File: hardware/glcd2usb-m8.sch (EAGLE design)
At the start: 19 parts, among them IC1 MEGA8-P, Q1 12MHz, T1 BC547

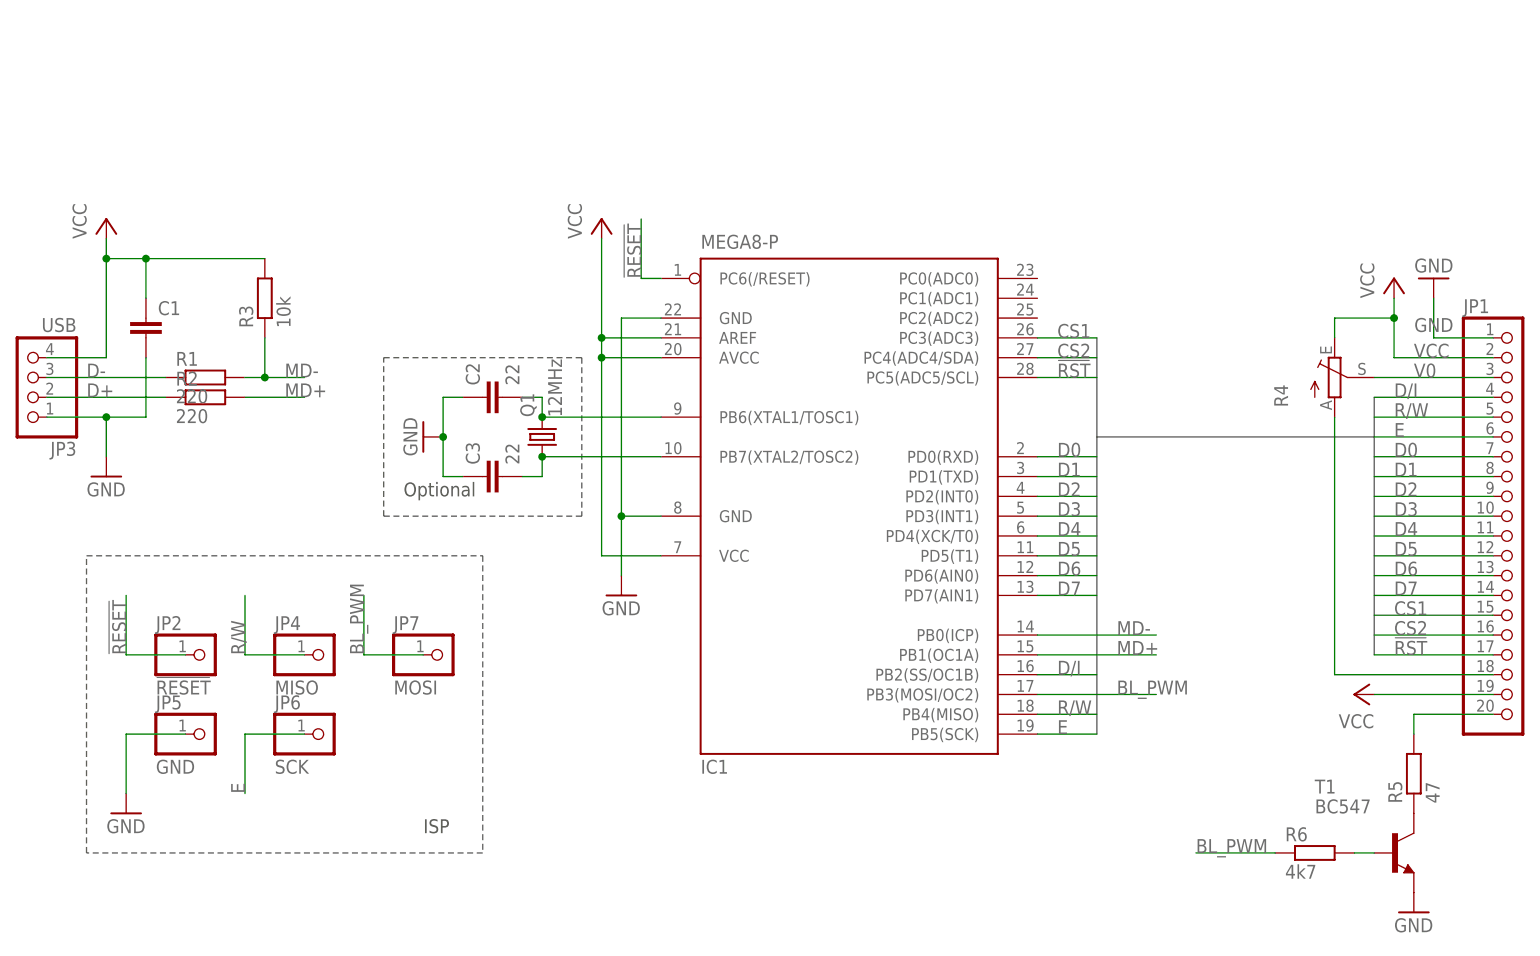
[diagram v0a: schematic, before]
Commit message: use PortC for contntrol (glcd lib limitations)
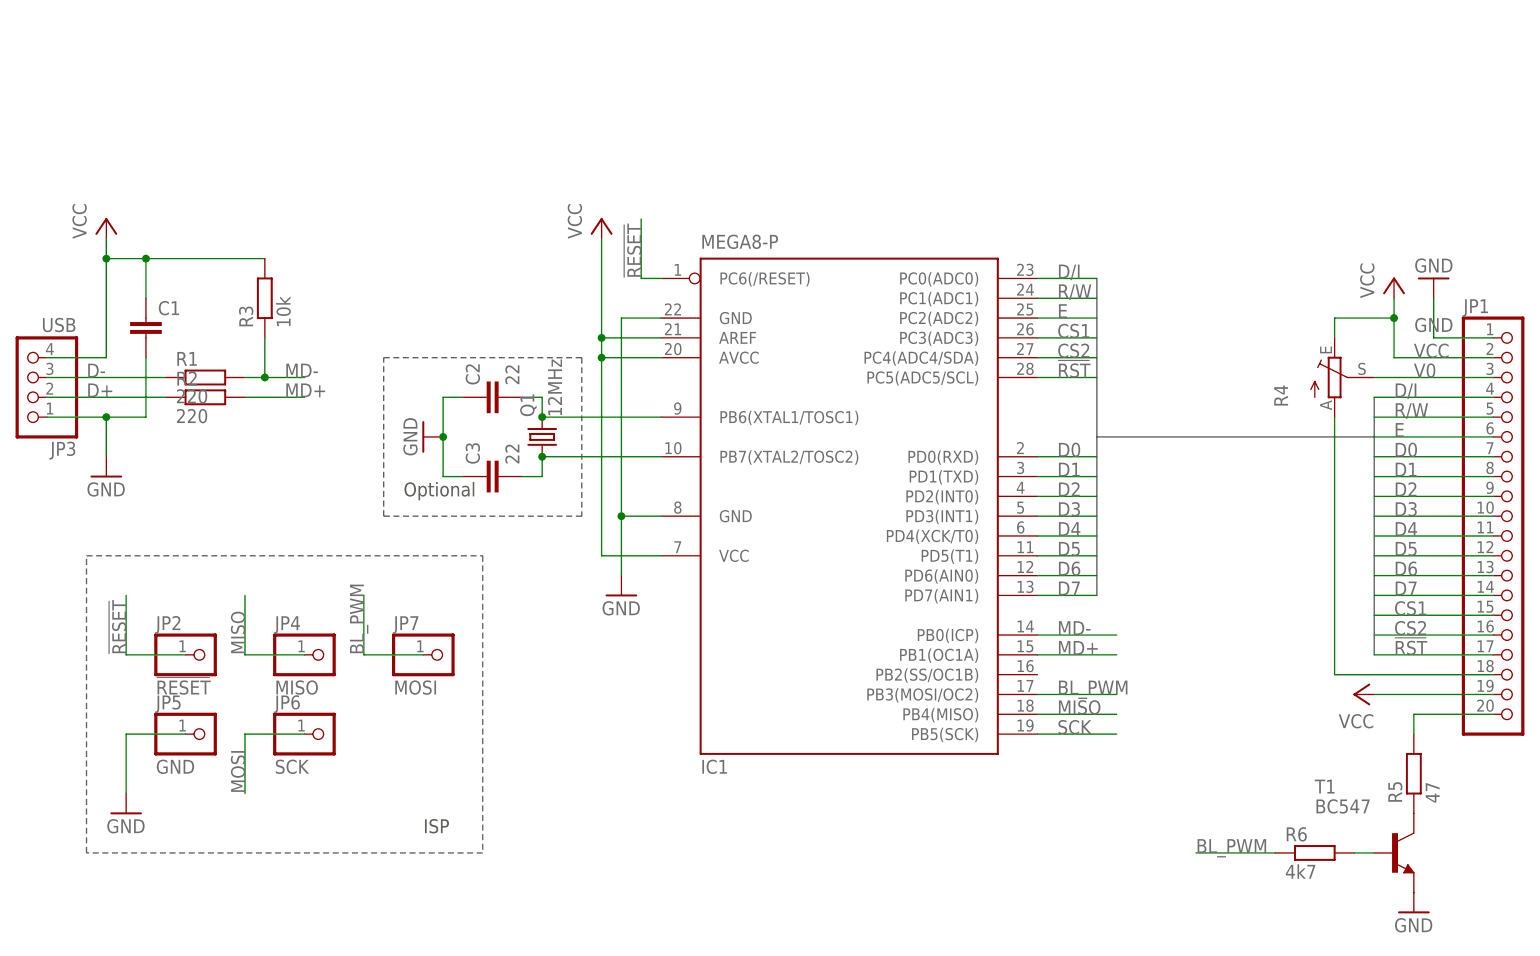
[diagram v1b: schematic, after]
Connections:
- new net MISO: IC1.PB4(MISO), JP4.1
- new net MOSI: JP6.1
- new net SCK: IC1.PB5(SCK)
- net D/I: now also IC1.PC0(ADC0); no longer IC1.PB2(SS/OC1B)
- net E: now also IC1.PC2(ADC2); no longer IC1.PB5(SCK), JP6.1
- net R/W: now also IC1.PC1(ADC1); no longer IC1.PB4(MISO), JP4.1
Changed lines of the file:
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@@
 <bus name="D0,D1,D2,D3,D4,D5,D6,D7,E,D/I,R/W,CS1,CS2,!RST">
 <segment>
-<wire x1="33.02" y1="-30.48" x2="33.02" y2="7.62" width="0.762" layer="92"/>
+<wire x1="33.02" y1="-12.7" x2="33.02" y2="7.62" width="0.762" layer="92"/>
 <wire x1="33.02" y1="7.62" x2="68.58" y2="7.62" width="0.762" layer="92"/>
 <wire x1="68.58" y1="7.62" x2="68.58" y2="-20.32" width="0.762" layer="92"/>
 <wire x1="68.58" y1="7.62" x2="68.58" y2="12.7" width="0.762" layer="92"/>
-<wire x1="33.02" y1="7.62" x2="33.02" y2="20.32" width="0.762" layer="92"/>
+<wire x1="33.02" y1="7.62" x2="33.02" y2="27.94" width="0.762" layer="92"/>
 </segment>
 </bus>
@@
 <segment>
 <pinref part="IC1" gate="G$1" pin="PB0(ICP)"/>
-<wire x1="25.4" y1="-17.78" x2="40.64" y2="-17.78" width="0.1524" layer="91"/>
-<label x="35.56" y="-17.78" size="1.778" layer="95"/>
+<wire x1="25.4" y1="-17.78" x2="35.56" y2="-17.78" width="0.1524" layer="91"/>
+<label x="27.94" y="-17.78" size="1.778" layer="95"/>
 </segment>
 </net>
@@
 <segment>
 <pinref part="IC1" gate="G$1" pin="PB1(OC1A)"/>
-<wire x1="25.4" y1="-20.32" x2="40.64" y2="-20.32" width="0.1524" layer="91"/>
-<label x="35.56" y="-20.32" size="1.778" layer="95"/>
+<wire x1="25.4" y1="-20.32" x2="35.56" y2="-20.32" width="0.1524" layer="91"/>
+<label x="27.94" y="-20.32" size="1.778" layer="95"/>
 </segment>
 </net>
@@
 <segment>
 <pinref part="IC1" gate="G$1" pin="PB3(MOSI/OC2)"/>
-<wire x1="25.4" y1="-25.4" x2="40.64" y2="-25.4" width="0.1524" layer="91"/>
-<label x="35.56" y="-25.4" size="1.778" layer="95"/>
+<wire x1="25.4" y1="-25.4" x2="35.56" y2="-25.4" width="0.1524" layer="91"/>
+<label x="27.94" y="-25.4" size="1.778" layer="95"/>
 </segment>
 <segment>
@@
 </segment>
 <segment>
+<pinref part="IC1" gate="G$1" pin="PC2(ADC2)"/>
+<wire x1="25.4" y1="22.86" x2="33.02" y2="22.86" width="0.1524" layer="91"/>
+<label x="27.94" y="22.86" size="1.778" layer="95"/>
+</segment>
+</net>
+<net name="D/I" class="0">
+<segment>
+<pinref part="JP1" gate="A" pin="4"/>
+<wire x1="83.82" y1="12.7" x2="68.58" y2="12.7" width="0.1524" layer="91"/>
+<label x="71.12" y="12.7" size="1.778" layer="95"/>
+</segment>
+<segment>
+<pinref part="IC1" gate="G$1" pin="PC0(ADC0)"/>
+<wire x1="25.4" y1="27.94" x2="33.02" y2="27.94" width="0.1524" layer="91"/>
+<label x="27.94" y="27.94" size="1.778" layer="95"/>
+</segment>
+</net>
+<net name="R/W" class="0">
+<segment>
+<pinref part="JP1" gate="A" pin="5"/>
+<wire x1="83.82" y1="10.16" x2="68.58" y2="10.16" width="0.1524" layer="91"/>
+<label x="71.12" y="10.16" size="1.778" layer="95"/>
+</segment>
+<segment>
+<pinref part="IC1" gate="G$1" pin="PC1(ADC1)"/>
+<wire x1="25.4" y1="25.4" x2="33.02" y2="25.4" width="0.1524" layer="91"/>
+<label x="27.94" y="25.4" size="1.778" layer="95"/>
+</segment>
+</net>
+<net name="CS1" class="0">
+<segment>
+<pinref part="JP1" gate="A" pin="15"/>
+<wire x1="83.82" y1="-15.24" x2="68.58" y2="-15.24" width="0.1524" layer="91"/>
+<label x="71.12" y="-15.24" size="1.778" layer="95"/>
+</segment>
+<segment>
+<pinref part="IC1" gate="G$1" pin="PC3(ADC3)"/>
+<wire x1="25.4" y1="20.32" x2="33.02" y2="20.32" width="0.1524" layer="91"/>
+<label x="27.94" y="20.32" size="1.778" layer="95"/>
+</segment>
+</net>
+<net name="CS2" class="0">
+<segment>
+<pinref part="JP1" gate="A" pin="16"/>
+<wire x1="83.82" y1="-17.78" x2="68.58" y2="-17.78" width="0.1524" layer="91"/>
+<label x="71.12" y="-17.78" size="1.778" layer="95"/>
+</segment>
+<segment>
+<pinref part="IC1" gate="G$1" pin="PC4(ADC4/SDA)"/>
+<wire x1="25.4" y1="17.78" x2="33.02" y2="17.78" width="0.1524" layer="91"/>
+<label x="27.94" y="17.78" size="1.778" layer="95"/>
+</segment>
+</net>
+<net name="!RST" class="0">
+<segment>
+<pinref part="JP1" gate="A" pin="17"/>
+<wire x1="83.82" y1="-20.32" x2="68.58" y2="-20.32" width="0.1524" layer="91"/>
+<label x="71.12" y="-20.32" size="1.778" layer="95"/>
+</segment>
+<segment>
+<pinref part="IC1" gate="G$1" pin="PC5(ADC5/SCL)"/>
+<wire x1="25.4" y1="15.24" x2="33.02" y2="15.24" width="0.1524" layer="91"/>
+<label x="27.94" y="15.24" size="1.778" layer="95"/>
+</segment>
+</net>
+<net name="!RESET" class="0">
+<segment>
+<pinref part="IC1" gate="G$1" pin="PC6(/RESET)"/>
+<wire x1="-22.86" y1="27.94" x2="-25.4" y2="27.94" width="0.1524" layer="91"/>
+<wire x1="-25.4" y1="27.94" x2="-25.4" y2="35.56" width="0.1524" layer="91"/>
+<label x="-25.4" y="27.94" size="1.778" layer="95" rot="R90"/>
+</segment>
+<segment>
+<pinref part="JP2" gate="G$1" pin="1"/>
+<wire x1="-83.82" y1="-20.32" x2="-91.44" y2="-20.32" width="0.1524" layer="91"/>
+<wire x1="-91.44" y1="-20.32" x2="-91.44" y2="-12.7" width="0.1524" layer="91"/>
+<label x="-91.44" y="-20.32" size="1.778" layer="95" rot="R90"/>
+</segment>
+</net>
+<net name="D-" class="0">
+<segment>
+<pinref part="R1" gate="G$1" pin="1"/>
+<pinref part="JP3" gate="A" pin="3"/>
+<wire x1="-86.36" y1="15.24" x2="-101.6" y2="15.24" width="0.1524" layer="91"/>
+<label x="-96.52" y="15.24" size="1.778" layer="95"/>
+</segment>
+</net>
+<net name="D+" class="0">
+<segment>
+<pinref part="R2" gate="G$1" pin="1"/>
+<pinref part="JP3" gate="A" pin="2"/>
+<wire x1="-86.36" y1="12.7" x2="-101.6" y2="12.7" width="0.1524" layer="91"/>
+<label x="-96.52" y="12.7" size="1.778" layer="95"/>
+</segment>
+</net>
+<net name="MISO" class="0">
+<segment>
+<pinref part="IC1" gate="G$1" pin="PB4(MISO)"/>
+<wire x1="25.4" y1="-27.94" x2="35.56" y2="-27.94" width="0.1524" layer="91"/>
+<label x="27.94" y="-27.94" size="1.778" layer="95"/>
+</segment>
+<segment>
+<pinref part="JP4" gate="G$1" pin="1"/>
+<wire x1="-68.58" y1="-20.32" x2="-76.2" y2="-20.32" width="0.1524" layer="91"/>
+<wire x1="-76.2" y1="-20.32" x2="-76.2" y2="-12.7" width="0.1524" layer="91"/>
+<label x="-76.2" y="-20.32" size="1.778" layer="95" rot="R90"/>
+</segment>
+</net>
+<net name="SCK" class="0">
+<segment>
 <pinref part="IC1" gate="G$1" pin="PB5(SCK)"/>
-<wire x1="25.4" y1="-30.48" x2="33.02" y2="-30.48" width="0.1524" layer="91"/>
+<wire x1="25.4" y1="-30.48" x2="35.56" y2="-30.48" width="0.1524" layer="91"/>
 <label x="27.94" y="-30.48" size="1.778" layer="95"/>
 </segment>
+</net>
+<net name="MOSI" class="0">
 <segment>
 <pinref part="JP6" gate="G$1" pin="1"/>
@@
 </segment>
 </net>
-<net name="D/I" class="0">
-<segment>
-<pinref part="JP1" gate="A" pin="4"/>
-<wire x1="83.82" y1="12.7" x2="68.58" y2="12.7" width="0.1524" layer="91"/>
-<label x="71.12" y="12.7" size="1.778" layer="95"/>
-</segment>
-<segment>
-<pinref part="IC1" gate="G$1" pin="PB2(SS/OC1B)"/>
-<wire x1="25.4" y1="-22.86" x2="33.02" y2="-22.86" width="0.1524" layer="91"/>
-<label x="27.94" y="-22.86" size="1.778" layer="95"/>
-</segment>
-</net>
-<net name="R/W" class="0">
-<segment>
-<pinref part="JP1" gate="A" pin="5"/>
-<wire x1="83.82" y1="10.16" x2="68.58" y2="10.16" width="0.1524" layer="91"/>
-<label x="71.12" y="10.16" size="1.778" layer="95"/>
-</segment>
-<segment>
-<pinref part="IC1" gate="G$1" pin="PB4(MISO)"/>
-<wire x1="25.4" y1="-27.94" x2="33.02" y2="-27.94" width="0.1524" layer="91"/>
-<label x="27.94" y="-27.94" size="1.778" layer="95"/>
-</segment>
-<segment>
-<pinref part="JP4" gate="G$1" pin="1"/>
-<wire x1="-68.58" y1="-20.32" x2="-76.2" y2="-20.32" width="0.1524" layer="91"/>
-<wire x1="-76.2" y1="-20.32" x2="-76.2" y2="-12.7" width="0.1524" layer="91"/>
-<label x="-76.2" y="-20.32" size="1.778" layer="95" rot="R90"/>
-</segment>
-</net>
-<net name="CS1" class="0">
-<segment>
-<pinref part="JP1" gate="A" pin="15"/>
-<wire x1="83.82" y1="-15.24" x2="68.58" y2="-15.24" width="0.1524" layer="91"/>
-<label x="71.12" y="-15.24" size="1.778" layer="95"/>
-</segment>
-<segment>
-<pinref part="IC1" gate="G$1" pin="PC3(ADC3)"/>
-<wire x1="25.4" y1="20.32" x2="33.02" y2="20.32" width="0.1524" layer="91"/>
-<label x="27.94" y="20.32" size="1.778" layer="95"/>
-</segment>
-</net>
-<net name="CS2" class="0">
-<segment>
-<pinref part="JP1" gate="A" pin="16"/>
-<wire x1="83.82" y1="-17.78" x2="68.58" y2="-17.78" width="0.1524" layer="91"/>
-<label x="71.12" y="-17.78" size="1.778" layer="95"/>
-</segment>
-<segment>
-<pinref part="IC1" gate="G$1" pin="PC4(ADC4/SDA)"/>
-<wire x1="25.4" y1="17.78" x2="33.02" y2="17.78" width="0.1524" layer="91"/>
-<label x="27.94" y="17.78" size="1.778" layer="95"/>
-</segment>
-</net>
-<net name="!RST" class="0">
-<segment>
-<pinref part="JP1" gate="A" pin="17"/>
-<wire x1="83.82" y1="-20.32" x2="68.58" y2="-20.32" width="0.1524" layer="91"/>
-<label x="71.12" y="-20.32" size="1.778" layer="95"/>
-</segment>
-<segment>
-<pinref part="IC1" gate="G$1" pin="PC5(ADC5/SCL)"/>
-<wire x1="25.4" y1="15.24" x2="33.02" y2="15.24" width="0.1524" layer="91"/>
-<label x="27.94" y="15.24" size="1.778" layer="95"/>
-</segment>
-</net>
-<net name="!RESET" class="0">
-<segment>
-<pinref part="IC1" gate="G$1" pin="PC6(/RESET)"/>
-<wire x1="-22.86" y1="27.94" x2="-25.4" y2="27.94" width="0.1524" layer="91"/>
-<wire x1="-25.4" y1="27.94" x2="-25.4" y2="35.56" width="0.1524" layer="91"/>
-<label x="-25.4" y="27.94" size="1.778" layer="95" rot="R90"/>
-</segment>
-<segment>
-<pinref part="JP2" gate="G$1" pin="1"/>
-<wire x1="-83.82" y1="-20.32" x2="-91.44" y2="-20.32" width="0.1524" layer="91"/>
-<wire x1="-91.44" y1="-20.32" x2="-91.44" y2="-12.7" width="0.1524" layer="91"/>
-<label x="-91.44" y="-20.32" size="1.778" layer="95" rot="R90"/>
-</segment>
-</net>
-<net name="D-" class="0">
-<segment>
-<pinref part="R1" gate="G$1" pin="1"/>
-<pinref part="JP3" gate="A" pin="3"/>
-<wire x1="-86.36" y1="15.24" x2="-101.6" y2="15.24" width="0.1524" layer="91"/>
-<label x="-96.52" y="15.24" size="1.778" layer="95"/>
-</segment>
-</net>
-<net name="D+" class="0">
-<segment>
-<pinref part="R2" gate="G$1" pin="1"/>
-<pinref part="JP3" gate="A" pin="2"/>
-<wire x1="-86.36" y1="12.7" x2="-101.6" y2="12.7" width="0.1524" layer="91"/>
-<label x="-96.52" y="12.7" size="1.778" layer="95"/>
-</segment>
-</net>
